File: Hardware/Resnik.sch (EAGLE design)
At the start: 179 parts, among them IC1 ATMEGA644M, J1 CONN_82.54_SCREW, J3 CONN_82.54_SCREW, J4 CONN_42.54_SCREW, Q1 DMG3404, Q2 DMG3404, Q3 FDN360P, Q4 FDN360P, Q5 FDN360P, Q6 DMG3404, U1 TLV61220DBV, U10 SN74AUP1G04YFP, U11 SN74AUP2G86SOT833-1, U12 SN74AUP2G08DQE, U13 SN74AUP2G08DQE, U14 SN74AUP2G08DQE, U15 MIC2039MT, U16 MIC2039MT, U17 MIC2039MT, U18 MIC2039MT, U19 TPS22917DBV, U2 TPS62822DLC, U20 TPS22917DBV, U21 TXS0102DQM, U22 BME280, U23 FT231X-Q, U24 TPS22917DBV, U25 TXS0108RGY, U26 TXS0108RGY, U27 TXS0104RGY, U28 MCP4726A2SOT-23, U29 ADS1115, U3 TPS61032RSA, U30 ADS1115, U31 INA211DCK, U32 INA210DCK, U33 TCA9555RTW, U5 BQ2980RUG, U6 TPS2105, U7 LTC4412S6, U8 TPS79733, U9 SN74AUP1G04YFP

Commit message: Minor board edits, updated gerbers, pending DFM
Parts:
- removed CX2, CX3: 12pF, bschulz_passives:C-EU12PFC0402
- removed D+, D-: 27, bschulz_passives:R-EU_27R0402
- removed H4: (no value), bschulz:MOUNTING_HOLE4_NP
- removed U$13: SN74LVC1G3157DRL, bschulz:SN74LVC1G3157DRL
- removed U$15, U$16: CLVBA-FKA, bschulz:CLVBA-FKA
- removed U$17: SN74AUP3G34DCU, bschulz:SN74AUP3G34DCU
- removed U$3: TPL5111DDC, bschulz:TPL5111DDC
- added C41: 12pF, bschulz_passives:C-EU12PFC0402
- added C42: 1uF, bschulz_passives:C-EU0.1UFC0402
- added D6, D7: (no value), bschulz:LM40402.5
- added H1: (no value), bschulz:MOUNTING_HOLE4_NP
- added R22: 10k, bschulz_passives:R-EU_R0402
- added R7: 180k, bschulz_passives:R-EU_R0603
- added U34: INA211DCK, bschulz:INA211DCK
- added U35: INA210DCK, bschulz:INA210DCK
- added U36: TCA9555RTW, bschulz:TCA9555RTW
- C22: value 0.1uF -> 10uF; device bschulz_passives:C-EU0.1UFC0402 -> bschulz_passives:C-EU10UFC0805
- C23: value 10uF -> 12pF; device bschulz_passives:C-EU10UFC0805 -> bschulz_passives:C-EU12PFC0402
- C24: value 0.1uF -> 12pF; device bschulz_passives:C-EU0.1UFC0402 -> bschulz_passives:C-EU12PFC0402
- C25: value 1uF -> 0.1uF; DIGIKEY 1276-6524-1-ND -> (none); MF Samsung -> (none); MPN CL10B105MO8NNWC -> (none)
- C26, C27: value 12pF -> (none); device bschulz_passives:C-EU12PFC0402 -> bschulz_passives:C-EUC0402; DIGIKEY 1276-1254-1-ND -> (none); MF Samsung -> (none); MPN CL10C120JB8NNNC -> (none)
- C28: value 0.1uF -> (none); device bschulz_passives:C-EU0.1UFC0402 -> bschulz_passives:C-EUC0402
- C32: device bschulz_passives:C-EUC0402 -> bschulz_passives:C-EU0.1UFC0402
- C34: value 0.1uF -> (none); device bschulz_passives:C-EUC0402 -> bschulz_passives:C-EU0.1UFC0402
- C37, C38: value (none) -> 0.1uF
- C39: value (none) -> 0.1uF; device bschulz_passives:C-EUC0402 -> bschulz_passives:C-EU0.1UFC0402
- C40: value (none) -> 12pF; device bschulz_passives:C-EU0.1UFC0402 -> bschulz_passives:C-EU12PFC0402; DIGIKEY (none) -> 1276-1254-1-ND; MF (none) -> Samsung; MPN (none) -> CL10C120JB8NNNC
- D1: device bschulz:DIODESOD-323 -> bschulz:DIODEDO-214AC
- D2: device bschulz:LM40402.5 -> bschulz:DIODESOD-323
- D3: device bschulz:LM40402.5 -> bschulz:DIODEDO-214AC
- D4, D5: value (none) -> CLVBA-FKA; device bschulz:DIODEDO-214AC -> bschulz:CLVBA-FKA
- J3: value CONN_82.54_SCREW -> CONN_42.54_SCREW; device bschulz:CONN_82.54_SCREW -> bschulz:CONN_42.54_SCREW
- J4: value CONN_42.54_SCREW -> CONN_82.54_SCREW; device bschulz:CONN_42.54_SCREW -> bschulz:CONN_82.54_SCREW
- Q3: device bschulz:MOSFET_PCH-FDN360P -> transistor-power:FDN360P
- Q5: device transistor-power:FDN360P -> bschulz:MOSFET_PCH-FDN360P
- R10: value 180k -> 3m; device bschulz_passives:R-EU_R0603 -> bschulz_passives:R-EU_R0805
- R11: value 330R -> 20R
- R12: value 3m -> (none); device bschulz_passives:R-EU_R0805 -> bschulz:R-EU_R0402
- R13: value 20R -> 91k; device bschulz:R-EU_R0402 -> bschulz_passives:R-EU_R0603
- R14: value (none) -> 100R
- R15: value 91k -> 2k
- R16: value 100R -> 182k; device bschulz:R-EU_R0402 -> bschulz_passives:R-EU_R0603
- R17: value 2k -> 330k
- R18: value 182k -> 5m; device bschulz_passives:R-EU_R0603 -> bschulz_passives:R-EU_R0805
- R19: value 330k -> 180k; device bschulz_passives:R-EU_R0603 -> bschulz_passives:R-EU_R0402
- R20: value 5m -> 120k; device bschulz_passives:R-EU_R0805 -> bschulz:R-EU_R0603
- R26: value 10k -> 287R
- R34: value 287R -> 27; device bschulz_passives:R-EU_R0402 -> bschulz_passives:R-EU_27R0402
- R35: value 330 -> 27; device bschulz_passives:R-EU_330R0402 -> bschulz_passives:R-EU_27R0402; MPN RC0603FR-07330RL -> (none)
- R36: DIGIKEY 311-330HRCT-ND -> (none); MF Yageo -> (none)
- R37: DIGIKEY (none) -> 311-330HRCT-ND
- R39: MF (none) -> Yageo
- R41: value 330 -> 10k; device bschulz_passives:R-EU_330R0402 -> bschulz_passives:R-EU_R0402; MPN RC0603FR-07330RL -> (none)
- R43, R44: value 10k -> 330; device bschulz_passives:R-EU_10KR0402 -> bschulz_passives:R-EU_330R0402; DIGIKEY 311-10.0KHRCT-ND -> (none); MPN (none) -> RC0603FR-07330RL
- R45: device bschulz_passives:R-EU_R0402 -> bschulz_passives:R-EU_10KR0402; DIGIKEY (none) -> 311-10.0KHRCT-ND
- R46: value 180k -> 10k
- R47: value 120k -> 10k; device bschulz:R-EU_R0603 -> bschulz_passives:R-EU_R0402
- R48: value 10k -> 330R; device bschulz_passives:R-EU_R0402 -> bschulz:R-EU_R0603
- R49: device bschulz_passives:R-EU_R0402 -> bschulz_passives:R-EU_P10KR0603
- R50: value 330R -> 10k; device bschulz:R-EU_R0603 -> bschulz_passives:R-EU_P10KR0603
- R52: device bschulz_passives:R-EU_P10KR0603 -> bschulz_passives:R-EU_10KR0402; DIGIKEY (none) -> 311-10.0KHRCT-ND
- R53: device bschulz_passives:R-EU_P10KR0603 -> bschulz_passives:R-EU_R0402
- R6: value 10k -> 820k; device bschulz_passives:R-EU_R0402 -> bschulz_passives:R-EU_R0603
- R8: value 820k -> 180k
- R9: value 180k -> 330R; device bschulz_passives:R-EU_R0603 -> bschulz:R-EU_R0402
- U10: value SN74AUP1G04YFP -> TPS22917DBV; device bschulz:SN74AUP1G04YFP -> bschulz:TPS22917DBV
- U11: value SN74AUP2G86SOT833-1 -> SN74AUP1G04YFP; device bschulz:SN74AUP2G86SOT833-1 -> bschulz:SN74AUP1G04YFP
- U12: value SN74AUP2G08DQE -> SN74AUP1G04YFP; device bschulz:SN74AUP2G08DQE -> bschulz:SN74AUP1G04YFP
- U13: value SN74AUP2G08DQE -> SN74AUP2G86SOT833-1; device bschulz:SN74AUP2G08DQE -> bschulz:SN74AUP2G86SOT833-1
- U15, U16: value MIC2039MT -> SN74AUP2G08DQE; device bschulz:MIC2039MT -> bschulz:SN74AUP2G08DQE
- U19, U20: value TPS22917DBV -> MIC2039MT; device bschulz:TPS22917DBV -> bschulz:MIC2039MT
- U21: value TXS0102DQM -> TPS22917DBV; device bschulz:TXS0102DQM -> bschulz:TPS22917DBV
- U22: value BME280 -> TPS22917DBV; device bschulz:BME280 -> bschulz:TPS22917DBV
- U24: value TPS22917DBV -> SN74LVC1G3157DRL; device bschulz:TPS22917DBV -> bschulz:SN74LVC1G3157DRL
- U25: value TXS0108RGY -> SN74AUP3G34DCU; device bschulz:TXS0108RGY -> bschulz:SN74AUP3G34DCU
- U26: value TXS0108RGY -> TXS0102DQM; device bschulz:TXS0108RGY -> bschulz:TXS0102DQM
- U27: value TXS0104RGY -> TXS0108RGY; device bschulz:TXS0104RGY -> bschulz:TXS0108RGY
- U28: value MCP4726A2SOT-23 -> TXS0108RGY; device bschulz:MCP4726A2SOT-23 -> bschulz:TXS0108RGY
- U29: value ADS1115 -> TXS0104RGY; device bschulz:ADS1115 -> bschulz:TXS0104RGY
- U30: value ADS1115 -> MCP4726A2SOT-23; device bschulz:ADS1115 -> bschulz:MCP4726A2SOT-23
- U31: value INA211DCK -> BME280; device bschulz:INA211DCK -> bschulz:BME280
- U32: value INA210DCK -> ADS1115; device bschulz:INA210DCK -> bschulz:ADS1115
- U33: value TCA9555RTW -> ADS1115; device bschulz:TCA9555RTW -> bschulz:ADS1115
- U8: value TPS79733 -> TPL5111DDC; device bschulz:TPS79733 -> bschulz:TPL5111DDC
- U9: value SN74AUP1G04YFP -> TPS79733; device bschulz:SN74AUP1G04YFP -> bschulz:TPS79733
- renumbered ISP2 to ISP1, MICRO_USB to USB1, U$1 to XTAL1, U$2 to SD1, U$5 to S3, U$9 to S4
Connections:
- new net N$1: USB1.BODY
- net 3V3_AUX: now also C26.1, C27.1, C28.1, C32.1, R24.2, R41.2, R46.2, R47.2, R6.2, U11.VCC, U14.VCC, U15.VCC, U20.VIN, U24.VCC, U25.VCC, U26.EN, U28.VA, U29.VA, U31.CSB, U31.SDO, U31.VDD, U31.VDDIO; no longer C21.1, C37.1, C38.1, C39.1, R26.2, R45.2, R48.2, R49.2, R8.2, U$13.VCC, U$17.VCC, U10.VCC, U13.VCC, U16.VIN, U21.EN, U21.VA, U22.CSB, U22.SDO, U22.VDD, U22.VDDIO, U25.VA, U9.VCC
- net 3V3_AUX_PG: now also U36.P13; no longer U33.P13
- net 3V3_CORE: now also C42.1, D4.ANODE, D5.ANODE, Q3.S, R19.2, R45.2, R52.2, R53.2, U13.VCC, U16.VCC, U36.VCC, U8.EN, U8.VDD, U9.VOUT; no longer C25.1, Q5.S, R43.2, R44.2, R46.2, R6.2, U$15.ANODE, U$16.ANODE, U$3.EN, U$3.VDD, U11.VCC, U14.VCC, U33.VCC, U8.VOUT
- net 3V3_FTDI: now also C25.1; no longer C24.1
- net 5V_AUX: now also C37.1, C38.1, R48.2, R8.2, U19.VIN, U26.VB, U32.VDD, U33.ADDR, U33.VDD, U34.V+, U35.V+; no longer C33.1, C34.1, R10.2, R50.2, U15.VIN, U21.VB, U28.VDD, U29.VDD, U30.ADDR, U31.V+, U32.V+
- net ADC_0: now also JP6.1, U33.AIN1; no longer JP7.1, U30.AIN1
- net ADC_1: now also U33.AIN0; no longer U30.AIN0
- net ADC_2: now also J4.5, U33.AIN2; no longer J3.5, U30.AIN2
- net ADC_3: now also J4.6, JP7.1, U33.AIN3; no longer J3.6, JP6.1, U30.AIN3
- net ADC_EXT_ALERT: now also U33.ALERT, U36.P7; no longer U30.ALERT, U33.P7
- net ADC_OB_ALERT: now also U32.ALERT, U36.P15; no longer U29.ALERT, U33.P15
- net ALIVE_LED: now also R37.2; no longer R39.2
- net BMS_CTR: now also R14.1, U36.P1; no longer R16.1, U33.P1
- net BUS_LOGIC_EN_PRIME: now also R46.1, U29.EN, U36.P6; no longer R48.1, U25.EN, U33.P6
- net BUS_LOGIC_EN_SEC: now also R47.1, U28.EN, U36.P10; no longer R49.1, U26.EN, U33.P10
- net C0: now also U13.A1, U13.B2, U16.B1; no longer U11.A1, U11.B2, U14.B1
- net C1: now also U13.A2, U13.B1, U16.B2; no longer U11.A2, U11.B1, U14.B2
- net CS_EXT: now also U27.A3; no longer U25.A3
- net CS_OUT: now also U27.B3; no longer U25.B3
- net DAC_OUT: now also C33.1, U30.VOUT; no longer C31.1, U28.VOUT
- net DTR: now also C39.1; no longer C28.1
- net EN_BUS_PRIME: now also R25.1, U15.A1, U15.B2; no longer R26.1, U13.A1, U13.B2
- net EN_BUS_SEC: now also R24.1, U14.A1, U14.B2; no longer R25.1, U12.A1, U12.B2
- net FAULT_PRIME: now also U19.!FAULT, U20.!FAULT, U36.P5; no longer U17.!FAULT, U18.!FAULT, U33.P5
- net FAULT_SEC: now also U17.!FAULT, U18.!FAULT, U36.P16; no longer U15.!FAULT, U16.!FAULT, U33.P16
- net FEATHER_BAT: now also U10.QOD, U10.VOUT; no longer U24.QOD, U24.VOUT
- net FEATHER_EN: now also Q3.G, R19.1, U36.P17; no longer Q5.G, R46.1, U33.P17
- net GLOBAL_INT: now also R53.1, U36.!INT; no longer R6.1, U33.!INT
- net GND: now also C23.1, C24.1, C26.2, C27.2, C28.2, C40.1, C41.1, C42.2, D6.A, D7.A, R10.2, R12.1, R17.2, R20.1, R22.1, R26.1, R27.2, R28.1, R29.2, R49.1, R50.1, R7.1, U28.GND, U30.VSS, U32.ADDR, U34.GND, U34.IN+, U35.GND, U35.REF, U36.A0, U36.A1, U36.A2, U36.GND; no longer C23.2, C24.2, C26.1, C27.1, C39.2, C40.2, CX2.1, CX3.1, D2.A, D4.A, R12.2, R14.1, R19.2, R24.1, R27.1, R28.2, R29.1, R30.2, R47.1, R52.1, R53.1, R9.1, U$13.GND, U$17.GND, U$3.GND, U28.VSS, U29.ADDR, U30.GND, U31.IN+, U32.REF, U33.A0, U33.A1, U33.A2
- net GPIO_0: now also U29.A1; no longer U27.A1
- net GPIO_0_OUT: now also U29.B1; no longer U27.B1
- net GPIO_1: now also U29.A2; no longer U27.A2
- net GPIO_1_OUT: now also U29.B2; no longer U27.B2
- net GPIO_2: now also U28.A4; no longer U26.A4
- net GPIO_2_OUT: now also J4.7, U28.B4; no longer J3.7, U26.B4
- net GPIO_3: now also U28.A3; no longer U26.A3
- net GPIO_3_OUT: now also J4.8, U28.B3; no longer J3.8, U26.B3
- net I_LI: now also U32.AIN3, U34.OUT; no longer U29.AIN3, U31.OUT
- net I_SOLAR: now also U32.AIN1, U35.OUT; no longer U29.AIN1, U32.OUT
- net LBI: now also R8.1, U36.P14; no longer R10.1, U33.P14
- net LED1: now also R44.1; no longer R42.1
- net LED2: now also R42.1; no longer R40.1
- net LED3: now also R43.1; no longer R41.1
- net LI+: now also R9.2, U32.AIN0; no longer R13.2, U29.AIN0
- net LI-: now also R10.1, U34.IN-; no longer R12.1, U31.IN-
- net LOG_INT: now also R45.1; no longer R43.1
- net MISO: now also U27.A4; no longer U25.A4
- net MISO_OUT: now also U27.B4; no longer U25.B4
- net MOSI: now also U25.1A, U27.A5; no longer U$17.1A, U25.A5
- net MOSI_BUF: now also U25.1Y; no longer U$17.1Y
- net MOSI_OUT: now also U27.B5; no longer U25.B5
- net MPPT_CHRG: now also U36.P3; no longer U33.P3
- net MPPT_FAULT: now also U36.P4; no longer U33.P4
- net MPPT_SHDN: now also U36.P2; no longer U33.P2
- net N$11: now also R15.2; no longer R17.2
- net N$12: now also R13.1, R16.2, R17.1; no longer R15.1, R18.2, R19.1
- net N$13: now also R12.2; no longer R16.2
- net N$14: now also R11.1; no longer R13.1
- net N$15: now also R13.2; no longer R15.2
- net N$16: now also R9.1; no longer R11.1
- net N$18: now also D2.C; no longer D1.C
- net N$20: now also D3.C; no longer D4.C
- net N$21: now also D7.C, U34.REF; no longer D3.C, U31.REF
- net N$22: now also U13.Y1, U16.A1; no longer U11.Y1, U14.A1
- net N$23: now also U16.Y1, U21.ON; no longer U14.Y1, U19.ON
- net N$24: now also U16.Y2, U22.ON; no longer U14.Y2, U20.ON
- net N$25: now also U13.Y2, U16.A2; no longer U11.Y2, U14.A2
- net N$26: now also U12.Y, U15.A2; no longer U10.Y, U13.A2
- net N$27: now also R28.2, R32.2, U19.ILIMIT; no longer R29.2, R33.2, U17.ILIMIT
- net N$28: now also R23.2, U12.A, U15.B1; no longer R24.2, U10.A, U13.B1
- net N$29: now also U15.Y1, U19.EN; no longer U13.Y1, U17.EN
- net N$3: now also R6.1, R7.2; no longer R8.1, R9.2
- net N$30: now also U15.Y2, U20.EN; no longer U13.Y2, U18.EN
- net N$31: now also R32.1; no longer R33.1
- net N$32: now also R33.2; no longer R34.2
- net N$33: now also R29.1, R33.1, U20.ILIMIT; no longer R30.1, R34.1, U18.ILIMIT
- net N$34: now also U11.Y, U14.A2; no longer U12.A2, U9.Y
- net N$35: now also R22.2, U11.A, U14.B1; no longer R23.2, U12.B1, U9.A
- net N$36: now also U14.Y1, U17.EN; no longer U12.Y1, U15.EN
- net N$37: now also U14.Y2, U18.EN; no longer U12.Y2, U16.EN
- net N$38: now also R26.2, R30.2, U17.ILIMIT; no longer R27.2, R31.2, U15.ILIMIT
- net N$39: now also R30.1; no longer R31.1
- net N$40: now also R31.2; no longer R32.2
- net N$41: now also R27.1, R31.1, U18.ILIMIT; no longer R28.1, R32.1, U16.ILIMIT
- net N$43: now also C34.1; no longer C40.1
- net N$45: now also Q5.G; no longer Q4.G
- net N$46: now also Q4.G; no longer Q3.G
- net N$47: now also R40.2; no longer R37.2
- net N$48: now also C24.2, R35.2; no longer CX3.2, D+.2
- net N$49: now also C23.2, R34.2; no longer CX2.2, D-.2
- net N$50: now also R35.1; no longer D+.1
- net N$51: now also R39.2; no longer R36.2
- net N$52: now also R34.1; no longer D-.1
- net N$53: now also D4.RED_CATH, R39.1; no longer R36.1, U$16.RED_CATH
- net N$54: now also D4.BLUE_CATH, R36.1; no longer R35.1, U$16.BLUE_CATH
- net N$56: now also D4.GREEN_CATH, R37.1; no longer R39.1, U$16.GREEN_CATH
- net N$57: now also R36.2; no longer R35.2
- net N$58: now also D5.BLUE_CATH, R42.2; no longer R40.2, U$15.BLUE_CATH
- net N$59: now also D5.GREEN_CATH, R43.2; no longer R41.2, U$15.GREEN_CATH
- net N$60: now also D5.RED_CATH, R44.2; no longer R42.2, U$15.RED_CATH
- net N$61: now also C40.2; no longer C27.2
- net N$62: now also C41.2; no longer C26.2
- net N$63: now also Q3.D, R20.2, U8.DELAY; no longer Q5.D, R47.2, U$3.DELAY
- net N$64: now also U10.ON, U8.DRVN; no longer U$3.DRVN, U24.ON
- net N$65: now also JP6.2, R49.2; no longer JP7.2, R53.2
- net N$66: now also JP7.2, R50.2; no longer JP6.2, R52.2
- net N$67: now also D1.C; no longer D5.C
- net PG_LDO: now also U36.P11, U9.PG; no longer U33.P11, U8.PG
- net RST: now also C39.2, R52.1; no longer C28.2, R44.1
- net RX_EXT: now also U28.A1, U29.A4; no longer U26.A1, U27.A4
- net RX_OUT_PRIME: now also U29.B4; no longer U27.B4
- net RX_OUT_SEC: now also J3.3, U28.B1; no longer J4.3, U26.B1
- net SCK: now also U25.2A, U27.A6; no longer U$17.2A, U25.A6
- net SCK_BUF: now also U25.2Y; no longer U$17.2Y
- net SCK_OUT: now also U27.B6; no longer U25.B6
- net SCL: now also U26.A2, U27.A2, U28.A5, U31.SCK, U36.SCL; no longer U21.A2, U22.SCK, U25.A2, U26.A5, U33.SCL
- net SCL_5V: now also U26.B2, U32.SCL, U33.SCL; no longer U21.B2, U28.SCL, U29.SCL
- net SCL_OUT_PRIME: now also U27.B2; no longer U25.B2
- net SCL_OUT_SEC: now also J4.4, U28.B5; no longer J3.4, U26.B5
- net SDA: now also U24.A; no longer U$13.A
- net SDA_5V: now also U26.B1, U32.SDA, U33.SDA; no longer U21.B1, U28.SDA, U29.SDA
- net SDA_CTRL: now also U24.S; no longer U$13.S
- net SDA_EXT: now also U24.B2, U27.A1, U28.A6; no longer U$13.B2, U25.A1, U26.A6
- net SDA_OB: now also U24.B1, U26.A1, U31.SDI, U36.SDA; no longer U$13.B1, U21.A1, U22.SDI, U33.SDA
- net SDA_OUT_PRIME: now also U27.B1; no longer U25.B1
- net SDA_OUT_SEC: now also J4.3, U28.B6; no longer J3.3, U26.B6
- net SD_CD: now also R41.1; no longer R45.1
- net SD_CS: now also U25.3A; no longer U$17.3A
- net SD_CS_BUF: now also U25.3Y; no longer U$17.3Y
- net SOLAR_SENSE+: now also R18.1, U35.IN+; no longer R20.1, U32.IN+
- net TX: now also R40.1; no longer R37.1
- net TX_EXT: now also U28.A2, U29.A3; no longer U26.A2, U27.A3
- net TX_OUT_PRIME: now also U29.B3; no longer U27.B3
- net TX_OUT_SEC: now also J3.4, U28.B2; no longer J4.4, U26.B2
- net VBUS_PRIME: now also U19.VOUT, U20.VOUT, U29.VB; no longer U17.VOUT, U18.VOUT, U25.VB
- net VBUS_SEC: now also U17.VOUT, U18.VOUT, U28.VB; no longer U15.VOUT, U16.VOUT, U26.VB
- net VREF: now also C31.1, D6.C, R48.1, U30.VREF; no longer C32.1, D2.C, R50.1, U28.VREF
- net VUSB: now also C21.1; no longer C23.1
- net VUSB_POWER: now also Q4.D, U36.P0; no longer Q3.D, U33.P0
- net V_BETA: now also Q5.S, U22.VIN; no longer Q3.S, U20.VIN
- net V_CORE: now also U9.VIN; no longer U8.VIN
- net V_HP: now also U21.QOD, U21.VOUT, U22.QOD, U22.VOUT; no longer U19.QOD, U19.VOUT, U20.QOD, U20.VOUT
- net V_HP_SYNC: now also U36.P12; no longer U33.P12
- net V_LI: now also D2.A, Q5.D, R15.1, R16.1, R18.2, U10.VIN, U35.IN-; no longer D1.A, Q4.D, R17.1, R18.1, R20.2, U24.VIN, U32.IN-
- net V_PRIME: now also U21.VIN, U32.AIN2; no longer U19.VIN, U29.AIN2
- net V_SOLAR: now also D1.A; no longer D5.A
- net WD_DONE: now also U8.DONE; no longer U$3.DONE

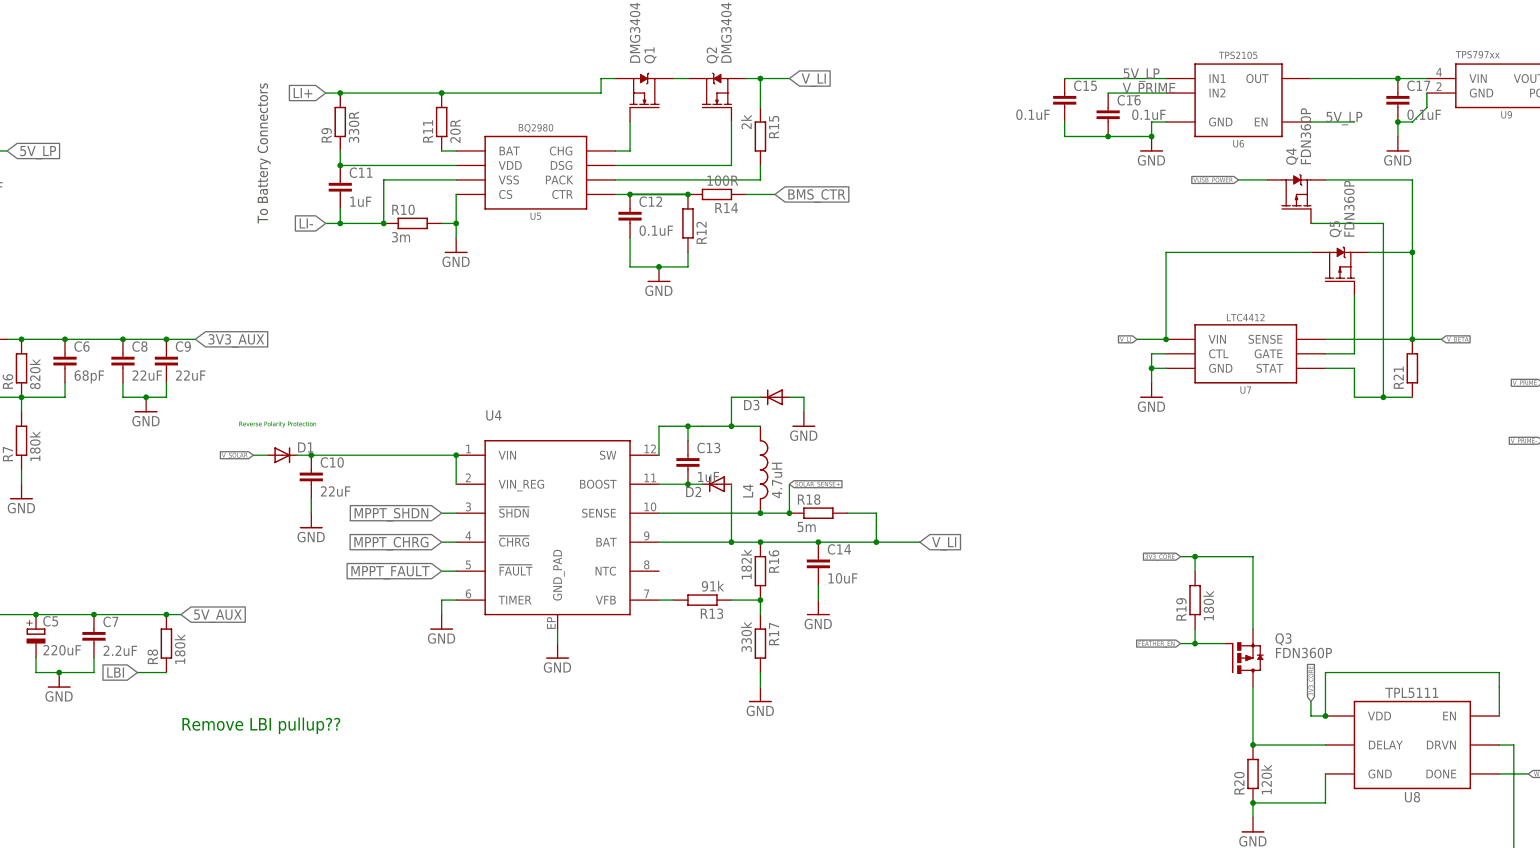
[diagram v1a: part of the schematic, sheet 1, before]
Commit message: Updated BOM info
Added info to schematic to support auto-generating BOM
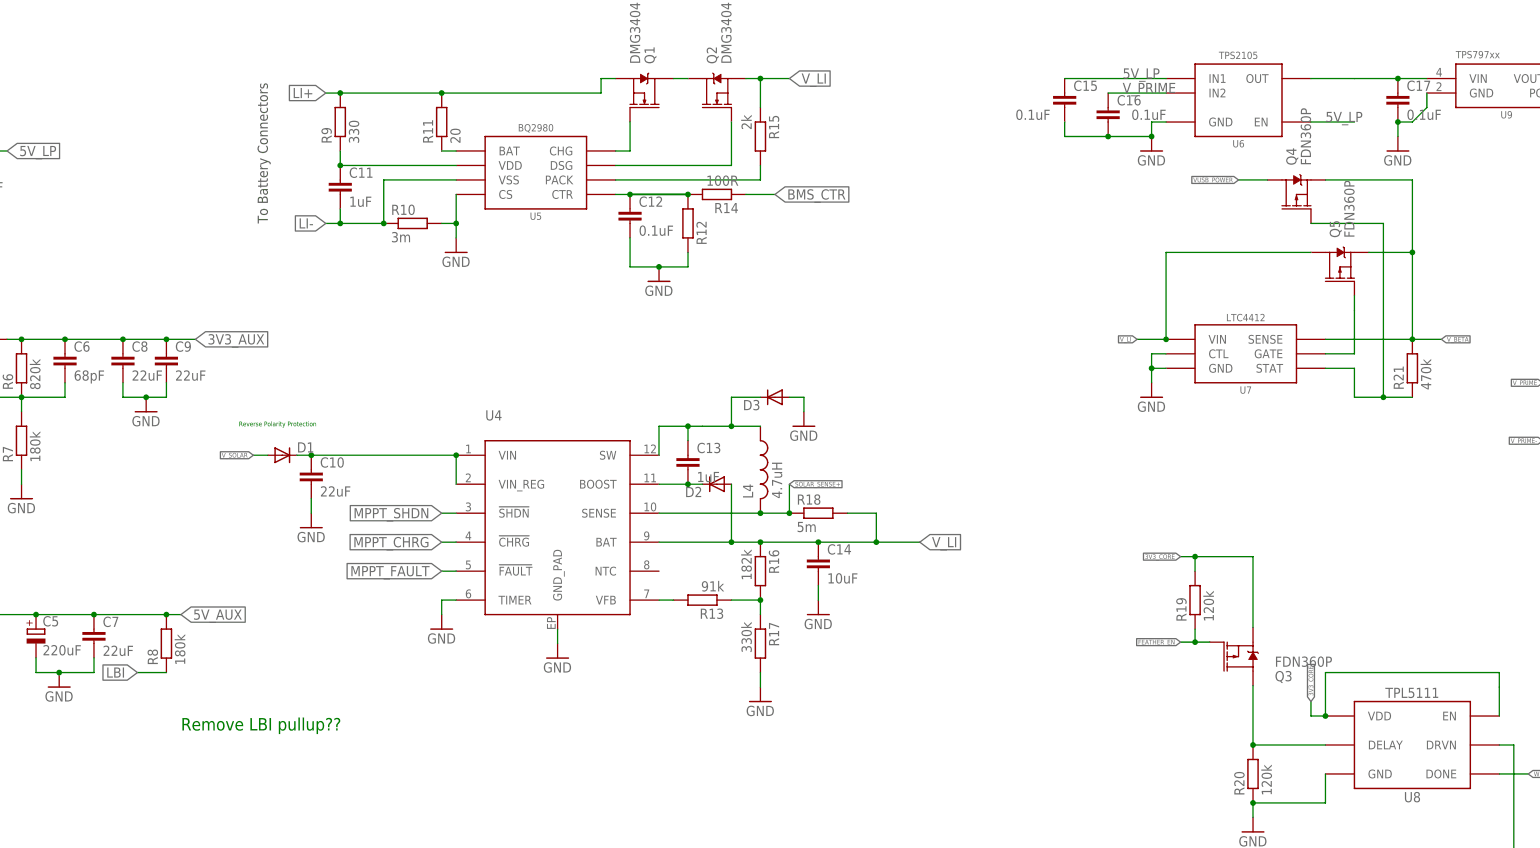
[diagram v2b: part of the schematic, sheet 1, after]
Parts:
- C1: device bschulz_passives:C-EUC0805 -> bschulz_passives:C-EU4.7UFC0805
- C10, C19, C2, C20, C8, C9: device bschulz_passives:C-EUC0805 -> bschulz_passives:C-EU22UFC0805
- C11, C13: device bschulz_passives:C-EUC0603 -> bschulz_passives:C-EU1UFC0603
- C12, C29, C31, C33, C35, C36, C37, C38: device bschulz_passives:C-EUC0402 -> bschulz_passives:C-EU0.1UFC0402
- C14, C3, C30, C4: device bschulz_passives:C-EUC0805 -> bschulz_passives:C-EU10UFC0805
- C26, C27, C28: value (none) -> 0.1uF; device bschulz_passives:C-EUC0402 -> bschulz_passives:C-EU0.1UFC0402
- C34: value (none) -> 0.1uF
- C5: DIGIKEY (none) -> 478-5408-1-ND; MF (none) -> AVX; MPN (none) -> TPSY227K010R0100
- C6: device bschulz_passives:C-EUC0402 -> bschulz_passives:C-EU68PFC0402
- C7: value 2.2uF -> 22uF; device bschulz_passives:C-EUC0805 -> bschulz_passives:C-EU22UFC0805
- D1, D3: DIGIKEY (none) -> CMSH3-40MATR13CT-ND; MF (none) -> Central Semiconductor; MPN (none) -> CMSH3-40MA TR13
- D2: DIGIKEY (none) -> CMDSH2-3CT-ND; MF (none) -> Central Semiconductor; MPN (none) -> CMDSH2-3 TR
- L1: DIGIKEY (none) -> 732-4849-1-ND; MF (none) -> Wurth; MPN (none) -> 74438323068
- L2: DIGIKEY (none) -> 732-1208-1-ND; MF (none) -> Wurth; MPN (none) -> 74477110
- L3: DIGIKEY (none) -> 732-5491-1-ND; MF (none) -> Wurth; MPN (none) -> 74404032010
- L4: DIGIKEY (none) -> 732-11316-1-ND; MF (none) -> Wurth; MPN (none) -> 78438356047
- Q3: device transistor-power:FDN360P -> bschulz:MOSFET_PCH-FDN360P
- R1, R5, R7, R8: device bschulz_passives:R-EU_R0603 -> bschulz_passives:R-EU_180KR0603
- R10: device bschulz_passives:R-EU_R0805 -> bschulz_passives:R-EU_0.003R0805
- R11: value 20R -> 20; device bschulz:R-EU_R0402 -> bschulz_passives:R-EU_20R0402
- R12: device bschulz:R-EU_R0402 -> bschulz_passives:R-EU_R0402
- R13: device bschulz_passives:R-EU_R0603 -> bschulz_passives:R-EU_91KR0603
- R14: device bschulz:R-EU_R0402 -> bschulz_passives:R-EU_100R0402
- R15: device bschulz_passives:R-EU_R0603 -> bschulz_passives:R-EU_2KR0402
- R16: device bschulz_passives:R-EU_R0603 -> bschulz_passives:R-EU_182KR0603
- R17: device bschulz_passives:R-EU_R0603 -> bschulz_passives:R-EU_330KR0603
- R18: device bschulz_passives:R-EU_R0805 -> bschulz_passives:R-EU_0.005R0805
- R19: value 180k -> 120k; device bschulz_passives:R-EU_R0402 -> bschulz_passives:R-EU_120KR0402
- R2, R4: device bschulz_passives:R-EU_R0603 -> bschulz_passives:R-EU_1.62MR0603
- R20: device bschulz:R-EU_R0603 -> bschulz_passives:R-EU_120KR0402
- R21: value (none) -> 470k; device bschulz:R-EU_R0603 -> bschulz_passives:R-EU_470KR0603
- R22, R23, R24, R25, R41, R46, R47, R53: device bschulz_passives:R-EU_R0402 -> bschulz_passives:R-EU_10KR0402
- R26, R27, R28, R29, R30, R31, R32, R33: device bschulz_passives:R-EU_R0402 -> bschulz_passives:R-EU_287R0402
- R3: device bschulz_passives:R-EU_R0603 -> bschulz_passives:R-EU_360KR0603
- R48: device bschulz:R-EU_R0603 -> bschulz:R-EU_330R0603
- R6: device bschulz_passives:R-EU_R0603 -> bschulz_passives:R-EU_820KR0603
- R9: value 330R -> 330; device bschulz:R-EU_R0402 -> bschulz_passives:R-EU_330R0402
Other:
- note added: "Check current rating!!"
